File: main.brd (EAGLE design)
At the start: 50.8 x 50.8 mm, 42 parts, among them U2 SN65HVD32_D_8

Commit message: Added IMU
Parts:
- added C4: 6.8n, resistor:C0603
- added C5, C8: 100n, resistor:C0603
- added IMU: BNO055, BNO055:LGA28R50P4X10_380X520X100
- added R38, R39: 1k, resistor:R0603
- added R4, R6: 10k, resistor:R0603
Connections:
- new net IMU_INT: IMU.14
- new net N$15: C8.1, IMU.9
- new net N$18: IMU.4, R6.2
- new net NRESET: IMU.11, R4.2
- new net PA16_SER1_I2C_SDA: IMU.20, MCU.25, R38.2
- new net PA17_SER1_I2C_SCL: IMU.19, MCU.26, R39.2
- net 3.3V: now also C4.1, C5.1, IMU.28, IMU.3, R38.1, R39.1, R4.1, R6.1
- net GND: now also C4.2, C5.2, C8.2, IMU.10, IMU.15, IMU.16, IMU.17, IMU.18, IMU.2, IMU.25, IMU.5, IMU.6
- net GPIO7: no longer MCU.26
- net GPIO8: no longer MCU.25
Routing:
- net GPIO7: track 18.5 -> 5.97 mm
- net GPIO8: track 19.4 -> 8.42 mm
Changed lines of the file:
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@@
 <drawing>
 <settings>
-<setting alwaysvectorfont="yes"/>
+<setting alwaysvectorfont="no"/>
 <setting keepoldvectorfont="yes"/>
 <setting verticaltext="up"/>
@@
 <element name="VIN" library="pinhead" package="1X02" value="" x="46.99" y="12.065" rot="R90"/>
 <element name="GPIO" library="pinhead" library_urn="urn:adsk.eagle:library:325" package="1X08" package3d_urn="urn:adsk.eagle:package:22409/2" value="" x="46.99" y="26.67" rot="R270"/>
+<element name="IMU" library="BNO055" package="LGA28R50P4X10_380X520X100" value="BNO055" x="3.1115" y="-8.1534">
+<attribute name="AVAILABILITY" value="Good" x="3.1115" y="-8.1534" size="1.778" layer="27" display="off"/>
+<attribute name="DESCRIPTION" value="IMU ACCEL/GYRO/MAG I2C 28LGA" x="3.1115" y="-8.1534" size="1.778" layer="27" display="off"/>
+<attribute name="MF" value="Bosch" x="3.1115" y="-8.1534" size="1.778" layer="27" display="off"/>
+<attribute name="MP" value="BNO055" x="3.1115" y="-8.1534" size="1.778" layer="27" display="off"/>
+<attribute name="PACKAGE" value="LGA-28 Bosch" x="3.1115" y="-8.1534" size="1.778" layer="27" display="off"/>
+<attribute name="PRICE" value="7.78 USD" x="3.1115" y="-8.1534" size="1.778" layer="27" display="off"/>
+</element>
+<element name="C5" library="resistor" package="C0603" value="100n" x="10.4902" y="-6.5786"/>
+<element name="C8" library="resistor" package="C0603" value="100n" x="2.5781" y="-14.4399"/>
+<element name="C4" library="resistor" package="C0603" value="6.8n" x="9.0932" y="-14.4399"/>
+<element name="R4" library="resistor" package="R0603" value="10k" x="10.6426" y="-19.3167"/>
+<element name="R6" library="resistor" package="R0603" value="10k" x="1.397" y="-24.1935"/>
+<element name="R38" library="resistor" package="R0603" value="1k" x="1.397" y="-19.3167"/>
+<element name="R39" library="resistor" package="R0603" value="1k" x="6.0198" y="-19.3167"/>
 </elements>
 <signals>
@@
 <wire x1="23.5204" y1="36.576" x2="23.5204" y2="38.7858" width="0.254" layer="1"/>
 <wire x1="23.5204" y1="38.7858" x2="23.495" y2="38.8112" width="0.254" layer="1"/>
+<contactref element="IMU" pad="28"/>
+<contactref element="IMU" pad="3"/>
+<contactref element="C5" pad="1"/>
+<contactref element="C4" pad="1"/>
+<contactref element="R4" pad="1"/>
+<contactref element="R6" pad="1"/>
+<contactref element="R39" pad="1"/>
+<contactref element="R38" pad="1"/>
+<wire x1="0.547" y1="-19.3167" x2="0.547" y2="-24.1935" width="0" layer="19" extent="1-1"/>
+<wire x1="5.1698" y1="-19.3167" x2="0.547" y2="-19.3167" width="0" layer="19" extent="1-1"/>
+<wire x1="9.7926" y1="-19.3167" x2="5.1698" y2="-19.3167" width="0" layer="19" extent="1-1"/>
+<wire x1="8.2432" y1="-14.4399" x2="9.7926" y2="-19.3167" width="0" layer="19" extent="1-1"/>
+<wire x1="9.6402" y1="-6.5786" x2="8.2432" y2="-14.4399" width="0" layer="19" extent="1-1"/>
+<wire x1="1.3615" y1="-6.5909" x2="9.6402" y2="-6.5786" width="0" layer="19" extent="1-1"/>
+<wire x1="0.799" y1="-7.9034" x2="1.3615" y2="-6.5909" width="0" layer="19" extent="1-1"/>
+<wire x1="13.6779" y1="14.9098" x2="9.6402" y2="-6.5786" width="0" layer="19" extent="1-16"/>
 </signal>
 <signal name="GND">
@@
 <wire x1="34.5186" y1="10.707" x2="32.9429" y2="10.707" width="0.4064" layer="1"/>
 <wire x1="32.9429" y1="10.707" x2="31.8627" y2="11.7872" width="0.4064" layer="1"/>
+<contactref element="IMU" pad="2"/>
+<contactref element="IMU" pad="25"/>
+<contactref element="C4" pad="2"/>
+<contactref element="C5" pad="2"/>
+<contactref element="IMU" pad="16"/>
+<contactref element="IMU" pad="15"/>
+<contactref element="IMU" pad="10"/>
+<contactref element="C8" pad="2"/>
+<contactref element="IMU" pad="18"/>
+<contactref element="IMU" pad="5"/>
+<contactref element="IMU" pad="6"/>
+<contactref element="IMU" pad="17"/>
+<wire x1="11.3402" y1="-6.5786" x2="11.938" y2="9.2329" width="0" layer="19" extent="1-1"/>
+<wire x1="5.424" y1="-7.9034" x2="11.3402" y2="-6.5786" width="0" layer="19" extent="1-1"/>
+<wire x1="5.424" y1="-8.4034" x2="5.424" y2="-7.9034" width="0" layer="19" extent="1-1"/>
+<wire x1="5.424" y1="-8.9034" x2="5.424" y2="-8.4034" width="0" layer="19" extent="1-1"/>
+<wire x1="5.3615" y1="-9.7159" x2="5.424" y2="-8.9034" width="0" layer="19" extent="1-1"/>
+<wire x1="2.8615" y1="-9.7159" x2="5.3615" y2="-9.7159" width="0" layer="19" extent="1-1"/>
+<wire x1="0.8615" y1="-9.7159" x2="2.8615" y2="-9.7159" width="0" layer="19" extent="1-1"/>
+<wire x1="0.799" y1="-8.9034" x2="0.8615" y2="-9.7159" width="0" layer="19" extent="1-1"/>
+<wire x1="0.799" y1="-7.4034" x2="0.799" y2="-8.9034" width="0" layer="19" extent="1-1"/>
+<wire x1="2.8615" y1="-6.5909" x2="0.799" y2="-7.4034" width="0" layer="19" extent="1-1"/>
+<wire x1="3.4281" y1="-14.4399" x2="2.8615" y2="-9.7159" width="0" layer="19" extent="1-1"/>
+<wire x1="9.9432" y1="-14.4399" x2="3.4281" y2="-14.4399" width="0" layer="19" extent="1-1"/>
 </signal>
 <signal name="VDDCORE">
@@
 <signal name="GPIO7">
 <contactref element="GPIO" pad="7"/>
-<contactref element="MCU" pad="26"/>
 <wire x1="46.99" y1="20.32" x2="45.0215" y2="20.32" width="0.254" layer="1"/>
-<wire x1="42.1915" y1="23.15" x2="29.65" y2="23.15" width="0.254" layer="1"/>
 <wire x1="45.0215" y1="20.32" x2="42.1915" y2="23.15" width="0.254" layer="1"/>
 </signal>
 <signal name="GPIO8">
 <contactref element="GPIO" pad="8"/>
-<contactref element="MCU" pad="25"/>
 <wire x1="46.99" y1="17.78" x2="45.4533" y2="17.78" width="0.254" layer="1"/>
-<wire x1="40.5833" y1="22.65" x2="29.65" y2="22.65" width="0.254" layer="1"/>
 <wire x1="45.4533" y1="17.78" x2="40.5833" y2="22.65" width="0.254" layer="1"/>
 </signal>
@@
 <wire x1="33.4563" y1="26.65" x2="29.65" y2="26.65" width="0.254" layer="1"/>
 </signal>
+<signal name="PA17_SER1_I2C_SCL">
+<contactref element="MCU" pad="26"/>
+<contactref element="IMU" pad="19"/>
+<contactref element="R39" pad="2"/>
+<wire x1="5.424" y1="-7.4034" x2="29.65" y2="23.15" width="0" layer="19" extent="1-1"/>
+<wire x1="6.8698" y1="-19.3167" x2="5.424" y2="-7.4034" width="0" layer="19" extent="1-1"/>
+</signal>
+<signal name="PA16_SER1_I2C_SDA">
+<contactref element="MCU" pad="25"/>
+<contactref element="IMU" pad="20"/>
+<contactref element="R38" pad="2"/>
+<wire x1="5.3615" y1="-6.5909" x2="29.65" y2="22.65" width="0" layer="19" extent="1-1"/>
+<wire x1="2.247" y1="-19.3167" x2="5.3615" y2="-6.5909" width="0" layer="19" extent="1-1"/>
+</signal>
+<signal name="NRESET">
+<contactref element="IMU" pad="11"/>
+<contactref element="R4" pad="2"/>
+<wire x1="3.3615" y1="-9.7159" x2="11.4926" y2="-19.3167" width="0" layer="19" extent="1-1"/>
+</signal>
+<signal name="N$15">
+<contactref element="IMU" pad="9"/>
+<contactref element="C8" pad="1"/>
+<wire x1="2.3615" y1="-9.7159" x2="1.7281" y2="-14.4399" width="0" layer="19" extent="1-1"/>
+</signal>
+<signal name="IMU_INT">
+<contactref element="IMU" pad="14"/>
+</signal>
+<signal name="N$18">
+<contactref element="IMU" pad="4"/>
+<contactref element="R6" pad="2"/>
+<wire x1="0.799" y1="-8.4034" x2="2.247" y2="-24.1935" width="0" layer="19" extent="1-1"/>
+</signal>
 </signals>

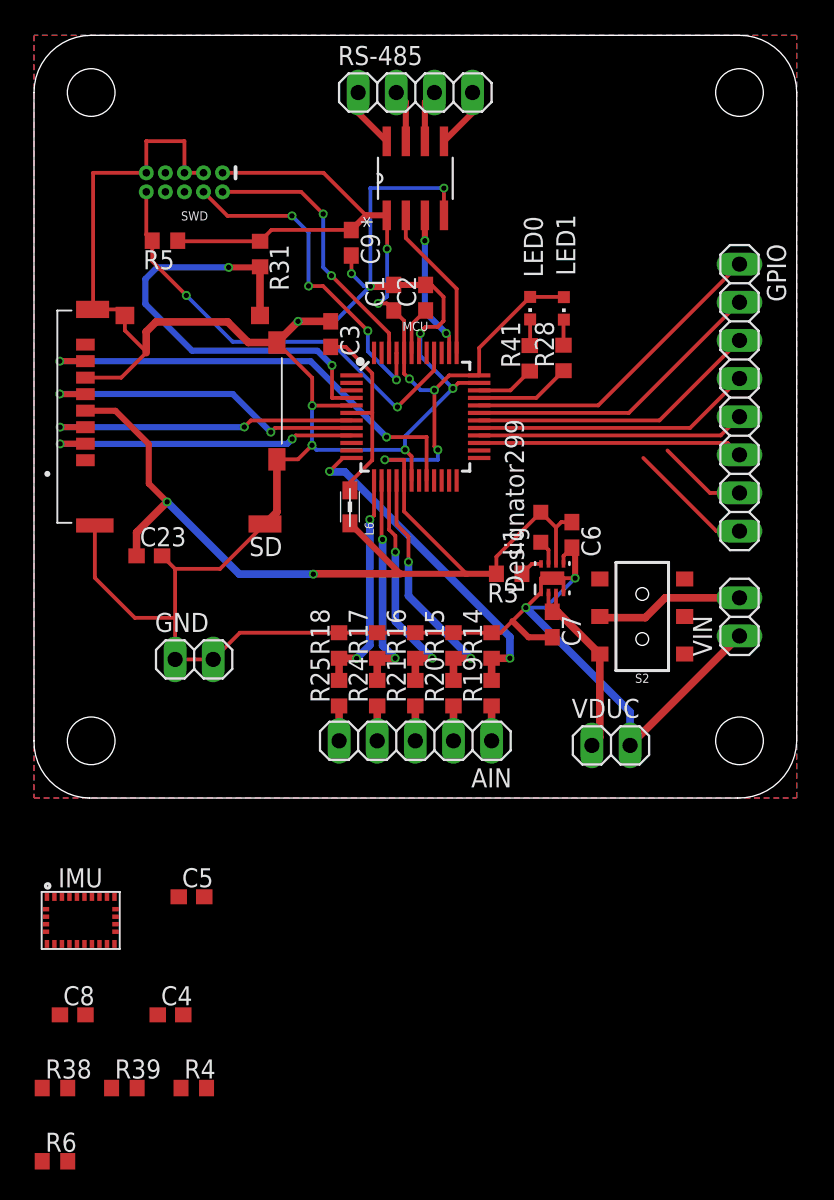
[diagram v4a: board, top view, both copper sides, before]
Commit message: Schematic and Layout Optimizations
Reconfigured a couple serial pins to make trace routing easier. Placed all compnents, just need to route and label.
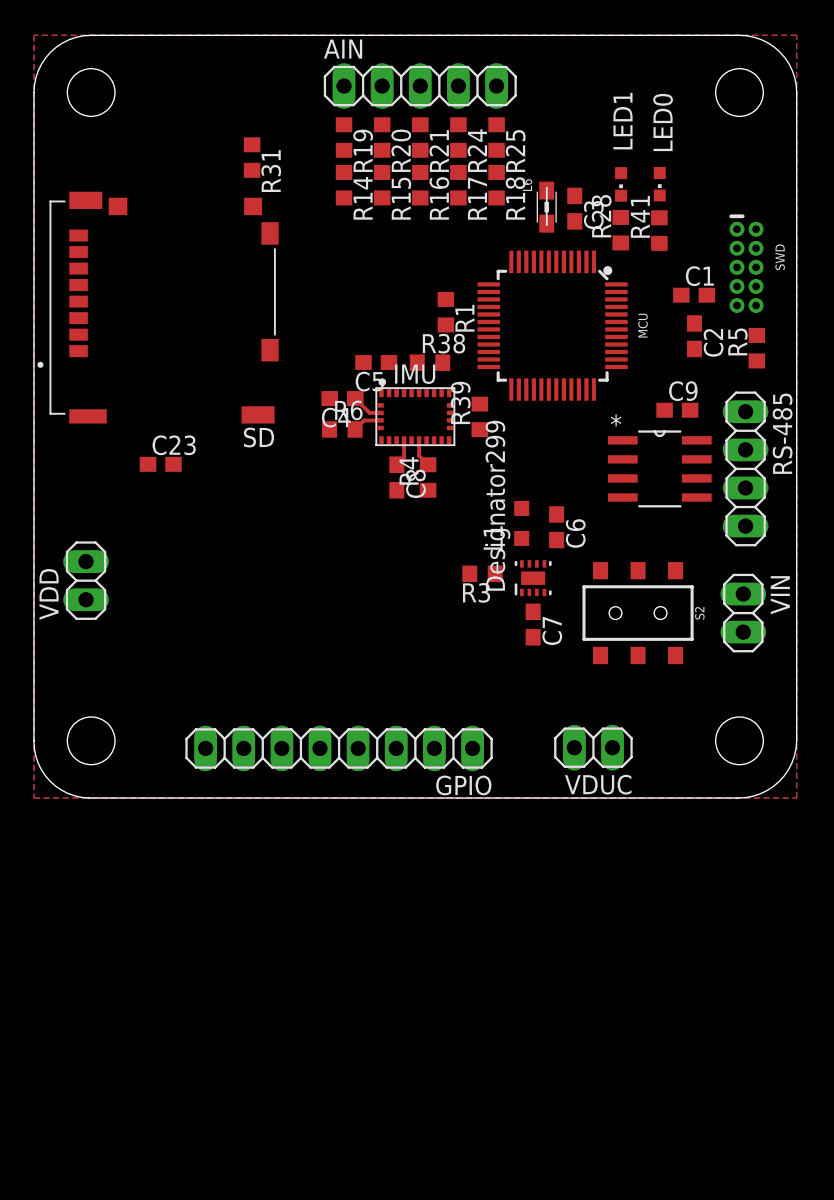
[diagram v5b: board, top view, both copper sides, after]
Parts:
- removed GND: (no value), pinhead:1X02
- added R1: 10k, resistor:R0603
- added VDD: (no value), pinhead:1X02
- moved R38 54.4 mm to (26.4, 29.0)
- moved R6 52.4 mm to (20.5, 24.5)
- moved R39 50.6 mm to (29.7, 25.4), turned to 90 degrees
- moved AIN 43.6 mm to (25.7, 47.4), turned to 0 degrees
- moved R4 43.6 mm to (26.3, 21.3), turned to 90 degrees
- moved C4 42.6 mm to (20.5, 26.6), turned to 180 degrees
- moved C8 41.8 mm to (24.2, 21.3), turned to 270 degrees
- moved IMU 40.3 mm to (25.4, 25.4)
- moved R5 40.1 mm to (48.1, 30.0), turned to 90 degrees
- moved R25 38.5 mm to (30.8, 44.0), turned to 270 degrees
- moved R19 38.3 mm to (20.7, 44.0), turned to 270 degrees
- moved SWD 37.9 mm to (47.5, 35.3), turned to 270 degrees
- moved C5 37.7 mm to (22.8, 29.0), turned to 180 degrees
- moved R24 37.4 mm to (28.3, 44.0), turned to 270 degrees
- moved R20 37.3 mm to (23.2, 44.0), turned to 270 degrees
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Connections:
- removed net N$10: MCU.34, R41.1
- removed net PB08D_SER4_P0: MCU.7, SD.3
- removed net PB09D_SER4_P1: MCU.8, SD.5
- removed net PB11D_SER4_P3: MCU.20, SD.7
- new net N$16: MCU.1, R41.1
- new net SER0_P0_DI: MCU.13, SD.7
- new net SER0_P1_CLK: MCU.14, SD.5
- new net SER0_P3_DO: MCU.16, SD.3
- net 3.3V: now also R1.1, VDD.1
- net AIN0: now also MCU.11; no longer MCU.12
- net AIN1: now also MCU.10; no longer MCU.16
- net AIN2: now also MCU.9; no longer MCU.15
- net AIN3: now also MCU.8; no longer MCU.14
- net AIN4: now also MCU.7; no longer MCU.13
- net GND: now also VDD.2; no longer GND.1, GND.2
- net GPIO1: now also MCU.39; no longer MCU.32
- net GPIO2: now also MCU.38; no longer MCU.31
- net GPIO3: now also MCU.37; no longer MCU.30
- net GPIO4: now also MCU.31; no longer MCU.29
- net GPIO5: now also MCU.30; no longer MCU.28
- net GPIO6: now also MCU.29; no longer MCU.27
- net GPIO7: now also MCU.28
- net GPIO8: now also MCU.27
- net MCU_RX: now also MCU.32; no longer MCU.38
- net MCU_TX: now also MCU.33; no longer MCU.37
- net N$14: now also MCU.2; no longer MCU.33
- net SD_CD: now also MCU.12; no longer MCU.4
- net SD_CS: now also MCU.21, R1.2; no longer MCU.9
- net VSYS: now also S2.3; no longer S2.1
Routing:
- net GND: track 205.0 -> 0.00 mm, vias 11 -> 0
- net 3.3V: track 123.9 -> 2.09 mm, vias 8 -> 0
- net PB11D_SER4_P3: track 31.1 -> 0.00 mm, vias 2 -> 0
- net SD_CD: track 30.5 -> 0.00 mm, vias 2 -> 0
- net SWD_NRES: track 29.8 -> 0.00 mm, vias 2 -> 0
- net PA30_SWCLK: track 22.7 -> 0.00 mm, vias 4 -> 0
- net AIN0: track 22.5 -> 0.00 mm, vias 2 -> 0
- net PB09D_SER4_P1: track 22.3 -> 0.00 mm, vias 2 -> 0
- net SD_CS: track 21.3 -> 0.00 mm, vias 2 -> 0
- net PB08D_SER4_P0: track 21.3 -> 0.00 mm, vias 2 -> 0
- net GPIO1: track 21.2 -> 0.00 mm
- net GPIO2: track 20.4 -> 0.00 mm
- net GPIO3: track 19.5 -> 0.00 mm
- net GPIO4: track 18.7 -> 0.00 mm
- net PA31_SWDIO: track 18.4 -> 0.00 mm, vias 2 -> 0
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
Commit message: Routed everything
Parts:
- moved R1 2.07 mm to (25.6, 31.5), turned to 0 degrees
- moved L6 1.48 mm to (34.9, 40.6)
- moved C3 1.27 mm to (36.8, 40.3)
- moved C5 1.27 mm to (21.8, 29.8)
- moved R6 1.27 mm to (19.8, 23.5)
- moved L1 0.92 mm to (31.7, 18.8)
- moved R39 0.92 mm to (30.2, 24.6)
- moved C6 0.80 mm to (35.1, 18.8)
- moved C4 0.80 mm to (19.8, 26.9)
- moved C7 0.76 mm to (33.2, 10.8)
- moved R3 0.76 mm to (29.1, 14.9)
- moved R4 0.72 mm to (26.8, 20.8)
- moved C8 0.57 mm to (23.9, 20.8)
- moved R38 0.25 mm to (26.4, 29.2)
- moved LED0 0.25 mm to (41.7, 41.1)
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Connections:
- net SD_CS: now also MCU.19; no longer MCU.21
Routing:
- net 3.3V: track 2.09 -> 115.7 mm, vias 0 -> 16
- net GND: track 0.00 -> 81.2 mm, vias 0 -> 27
- net GPIO1: track 0.00 -> 38.3 mm, vias 0 -> 1
- net GPIO8: track 0.00 -> 36.8 mm, vias 0 -> 1
- net GPIO2: track 0.00 -> 36.6 mm, vias 0 -> 1
- net GPIO7: track 0.00 -> 32.8 mm, vias 0 -> 1
- net GPIO3: track 0.00 -> 32.4 mm, vias 0 -> 1
- net SD_CS: track 0.00 -> 32.0 mm, vias 0 -> 2
- net GPIO6: track 0.00 -> 31.3 mm, vias 0 -> 1
- net SER0_P0_DI: track 0.00 -> 31.1 mm, vias 0 -> 2
- net SER0_P3_DO: track 0.00 -> 30.6 mm, vias 0 -> 2
- net SER0_P1_CLK: track 0.00 -> 30.4 mm, vias 0 -> 2
- net GPIO5: track 0.00 -> 30.3 mm, vias 0 -> 1
- net GPIO4: track 0.00 -> 29.4 mm, vias 0 -> 1
- net SD_CD: track 0.00 -> 21.2 mm
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- added copper zone on layer 15, net 3.3V
- added copper zone on layer 2, net GND

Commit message: Small tweaks before labels
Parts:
- added FUNC: (no value), SparkFun-Switches:SWITCH_DPDT_SMD_AYZ0202
- added R2: 10k, resistor:R0603
- renumbered S2 to PWR
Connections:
- net 3.3V: now also R2.1
- net GND: now also FUNC.3
- net GPIO8: now also FUNC.2, R2.2
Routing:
- net GPIO8: track 36.8 -> 50.6 mm, vias 1 -> 2
- net GND: track 81.2 -> 84.8 mm, vias 27 -> 38
- net 3.3V: track 115.7 -> 118.0 mm, vias 16 -> 17
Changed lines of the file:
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@@
 <element name="L1" library="resistor" package="L2012C" value="2.2u" x="31.7246" y="18.796" rot="R90"/>
 <element name="C6" library="resistor" package="C0603" value="22u" x="35.0647" y="18.796" rot="R270"/>
-<element name="S2" library="SparkFun-Switches" package="SWITCH_DPDT_SMD_AYZ0202" value="" x="40.2336" y="12.319" rot="R180">
+<element name="PWR" library="SparkFun-Switches" package="SWITCH_DPDT_SMD_AYZ0202" value="" x="40.2336" y="12.319" rot="R180">
 <attribute name="PROD_ID" value="SWCH-08179" x="49.5808" y="25.1079" size="1.778" layer="27" rot="R180" display="off"/>
 <attribute name="SF_ID" value="COM-00597" x="49.5808" y="25.1079" size="1.778" layer="27" rot="R180" display="off"/>
@@
 <element name="R39" library="resistor" package="R0603" value="1k" x="30.2006" y="24.6253" rot="R90"/>
 <element name="R1" library="resistor" package="R0603" value="10k" x="25.5524" y="31.496"/>
+<element name="FUNC" library="SparkFun-Switches" package="SWITCH_DPDT_SMD_AYZ0202" value="" x="13.208" y="13.589">
+<attribute name="PROD_ID" value="SWCH-08179" x="13.208" y="13.589" size="1.778" layer="27" display="off"/>
+<attribute name="SF_ID" value="COM-00597" x="13.208" y="13.589" size="1.778" layer="27" display="off"/>
+</element>
+<element name="R2" library="resistor" package="R0603" value="10k" x="13.208" y="19.05" rot="R270"/>
 </elements>
 <signals>
@@
 <wire x1="1.5684" y1="33.0644" x2="1.524" y2="33.02" width="0.254" layer="1"/>
 <via x="1.524" y="33.02" extent="1-16" drill="0.35"/>
+<contactref element="R2" pad="1"/>
+<wire x1="13.208" y1="19.9" x2="13.931" y2="19.9" width="0.254" layer="1"/>
+<wire x1="13.931" y1="19.9" x2="14.986" y2="20.955" width="0.254" layer="1"/>
+<via x="14.986" y="20.955" extent="1-16" drill="0.35"/>
 </signal>
 <signal name="GND">
@@
 <vertex x="0" y="50.8"/>
 </polygon>
-<wire x1="25.15" y1="26.9625" x2="25.15" y2="26.166" width="0.254" layer="1"/>
-<wire x1="25.15" y1="26.166" x2="25.146" y2="26.162" width="0.254" layer="1"/>
-<via x="25.146" y="26.162" extent="1-16" drill="0.35"/>
-<wire x1="23.0875" y1="26.15" x2="25.134" y2="26.15" width="0.254" layer="1"/>
-<wire x1="25.134" y1="26.15" x2="25.146" y2="26.162" width="0.254" layer="1"/>
 <wire x1="27.7125" y1="25.65" x2="26.797" y2="25.65" width="0.254" layer="1"/>
 <wire x1="26.797" y1="25.65" x2="26.547" y2="25.65" width="0.254" layer="1"/>
@@
 <wire x1="45.5032" y1="32.8041" x2="44.8174" y2="33.4899" width="0.254" layer="1"/>
 <wire x1="46.8249" y1="35.3441" x2="46.8249" y2="36.6141" width="0.254" layer="1"/>
-<wire x1="9.2955" y1="22.225" x2="10.287" y2="22.225" width="0.254" layer="1"/>
-<wire x1="10.287" y1="22.225" x2="10.541" y2="21.971" width="0.254" layer="1"/>
-<via x="10.541" y="21.971" extent="1-16" drill="0.35"/>
 <wire x1="14.9268" y1="25.5194" x2="14.9268" y2="23.9438" width="0.254" layer="1"/>
 <wire x1="14.9268" y1="23.9438" x2="14.351" y2="23.368" width="0.254" layer="1"/>
@@
 <wire x1="33.2486" y1="8.5344" x2="34.036" y2="7.747" width="0.6096" layer="1"/>
 <via x="34.036" y="7.747" extent="1-16" drill="0.35"/>
+<via x="40.513" y="34.798" extent="1-16" drill="0.35"/>
+<contactref element="FUNC" pad="3"/>
+<wire x1="15.708" y1="16.414" x2="15.708" y2="17.994" width="0.254" layer="1"/>
+<wire x1="15.708" y1="17.994" x2="16.256" y2="18.542" width="0.254" layer="1"/>
+<via x="16.256" y="18.542" extent="1-16" drill="0.35"/>
+<via x="7.112" y="9.398" extent="1-16" drill="0.35"/>
+<via x="6.985" y="14.478" extent="1-16" drill="0.35"/>
+<via x="4.445" y="20.066" extent="1-16" drill="0.35"/>
+<via x="3.302" y="8.636" extent="1-16" drill="0.35"/>
+<via x="8.128" y="5.334" extent="1-16" drill="0.35"/>
+<via x="32.639" y="5.842" extent="1-16" drill="0.35"/>
+<via x="43.053" y="3.937" extent="1-16" drill="0.35"/>
+<via x="17.653" y="33.02" extent="1-16" drill="0.35"/>
+<via x="10.033" y="46.355" extent="1-16" drill="0.35"/>
+<via x="36.195" y="46.609" extent="1-16" drill="0.35"/>
+<via x="44.323" y="44.069" extent="1-16" drill="0.35"/>
+<wire x1="23.0875" y1="26.15" x2="23.761" y2="26.15" width="0.254" layer="1"/>
+<wire x1="23.761" y1="26.15" x2="24.892" y2="25.019" width="0.254" layer="1"/>
+<wire x1="25.15" y1="26.9625" x2="25.15" y2="25.908" width="0.254" layer="1"/>
+<wire x1="25.15" y1="25.908" x2="25.15" y2="25.277" width="0.254" layer="1"/>
+<wire x1="25.15" y1="25.277" x2="24.892" y2="25.019" width="0.254" layer="1"/>
+<wire x1="25.15" y1="25.908" x2="26.289" y2="25.908" width="0.254" layer="1"/>
 </signal>
 <signal name="VDDCORE">
@@
 <contactref element="TPS62162-Q1" pad="3"/>
 <contactref element="C7" pad="1"/>
-<contactref element="S2" pad="3"/>
+<contactref element="PWR" pad="3"/>
 <wire x1="33.2486" y1="11.645" x2="33.4986" y2="11.895" width="0.254" layer="1"/>
 <wire x1="33.4986" y1="11.895" x2="33.4986" y2="13.6931" width="0.254" layer="1"/>
@@
 </signal>
 <signal name="N$9">
-<contactref element="S2" pad="2"/>
+<contactref element="PWR" pad="2"/>
 <contactref element="VIN" pad="2"/>
 <wire x1="40.2336" y1="9.494" x2="42.1076" y2="7.62" width="0.6096" layer="1"/>
@@
 <wire x1="32.766" y1="29.21" x2="32.794" y2="29.182" width="0.254" layer="1"/>
 <wire x1="32.794" y1="29.182" x2="32.794" y2="27.2079" width="0.254" layer="1"/>
-<wire x1="11.43" y1="7.874" x2="32.766" y2="29.21" width="0.6096" layer="16"/>
+<wire x1="11.43" y1="7.874" x2="20.3835" y2="16.8275" width="0.6096" layer="16"/>
+<contactref element="FUNC" pad="2"/>
+<contactref element="R2" pad="2"/>
+<wire x1="20.3835" y1="16.8275" x2="32.766" y2="29.21" width="0.6096" layer="16"/>
+<wire x1="20.3835" y1="16.8275" x2="12.3825" y2="16.8275" width="0.6096" layer="16"/>
+<wire x1="12.3825" y1="16.8275" x2="11.049" y2="18.161" width="0.6096" layer="16"/>
+<via x="11.049" y="18.161" extent="1-16" drill="0.35"/>
+<wire x1="11.049" y1="18.161" x2="13.169" y2="18.161" width="0.6096" layer="1"/>
+<wire x1="13.169" y1="18.161" x2="13.208" y2="18.2" width="0.6096" layer="1"/>
+<wire x1="13.208" y1="18.2" x2="13.208" y2="16.414" width="0.6096" layer="1"/>
 </signal>
 <signal name="N$7">
